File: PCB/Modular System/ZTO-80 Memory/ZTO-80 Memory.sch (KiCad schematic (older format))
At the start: 10 parts, among them J1 ZTO-80 Bus, J2 Conn_01x02, U1 28C256, U2 AS6C62256, U3 74HC139

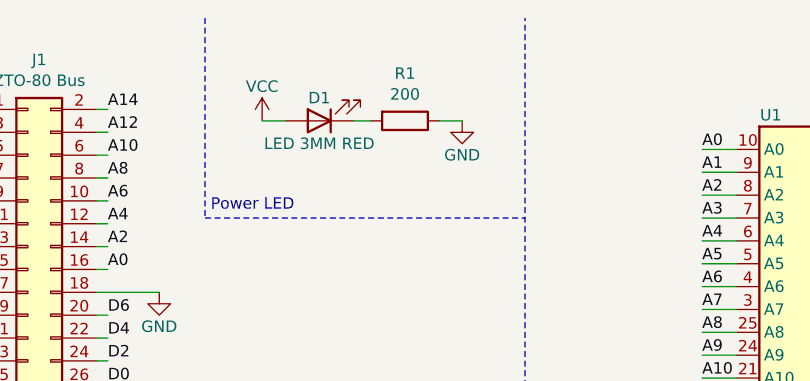
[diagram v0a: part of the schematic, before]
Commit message: Edited power LED resistor value
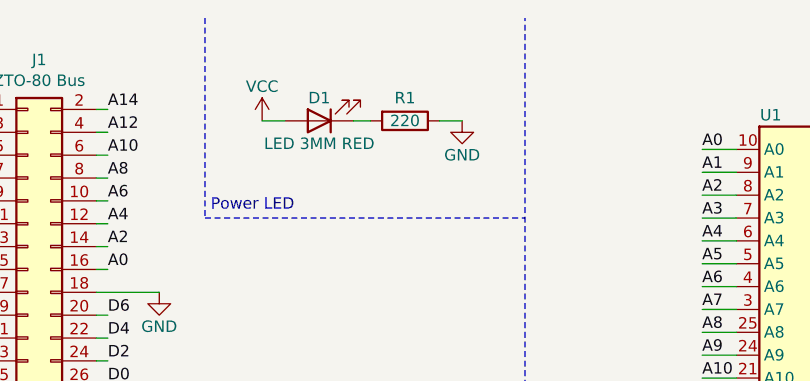
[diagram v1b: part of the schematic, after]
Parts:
- R1: value 200 -> 220
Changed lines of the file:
@@
 U 1 1 5E2B6523
 P 2825 925
-F 0 "R1" V 2618 925 50  0000 C CNN
-F 1 "200" V 2709 925 50  0000 C CNN
+F 0 "R1" V 2725 925 50  0000 C CNN
+F 1 "220" V 2825 925 50  0000 C CNN
 F 2 "Resistor_SMD:R_0805_2012Metric_Pad1.15x1.40mm_HandSolder" V 2755 925 50  0001 C CNN
 F 3 "~" H 2825 925 50  0001 C CNN

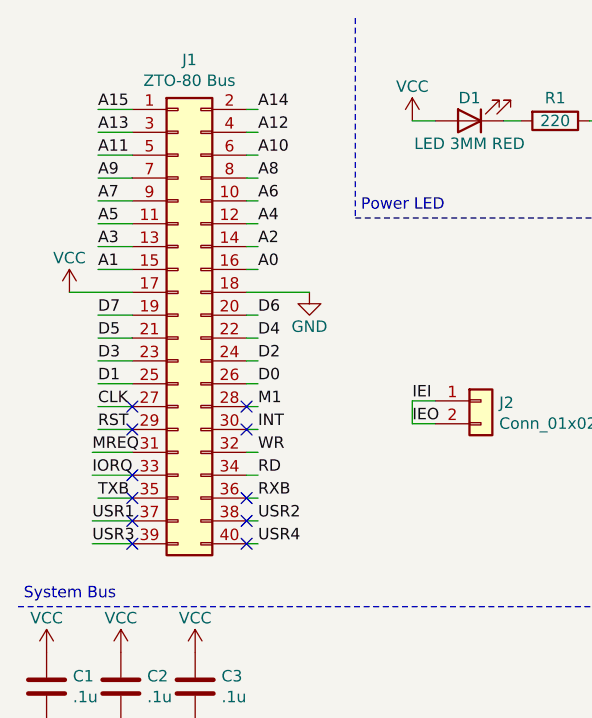
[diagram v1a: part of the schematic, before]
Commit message: Changed bus orientation
This change is backwards-compatible with all previous ZTO-80 modules
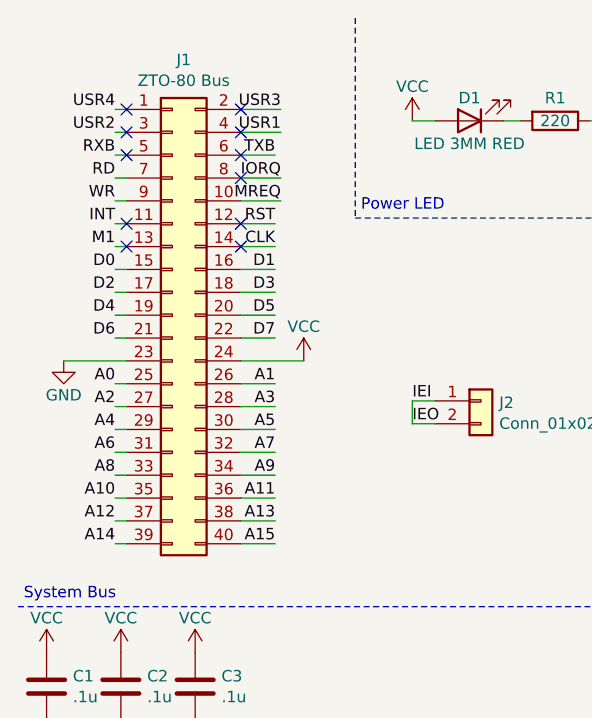
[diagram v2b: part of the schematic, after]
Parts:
- J1: footprint ZTO-80_Header:PinHeader_2x20_P2.54mm_Horizontal -> Connector_PinHeader_2.54mm:PinHeader_2x20_P2.54mm_Horizontal
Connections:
- net A0: now also J1.25 (Pin_25); no longer J1.16 (Pin_16)
- net A1: now also J1.26 (Pin_26); no longer J1.15 (Pin_15)
- net A10: now also J1.35 (Pin_35); no longer J1.6 (Pin_6)
- net A11: now also J1.36 (Pin_36); no longer J1.5 (Pin_5)
- net A12: now also J1.37 (Pin_37); no longer J1.4 (Pin_4)
- net A13: now also J1.38 (Pin_38); no longer J1.3 (Pin_3)
- net A14: now also J1.39 (Pin_39); no longer J1.2 (Pin_2)
- net A15: now also J1.40 (Pin_40); no longer J1.1 (Pin_1)
- net A2: now also J1.27 (Pin_27); no longer J1.14 (Pin_14)
- net A3: now also J1.28 (Pin_28); no longer J1.13 (Pin_13)
- net A4: now also J1.29 (Pin_29); no longer J1.12 (Pin_12)
- net A5: now also J1.30 (Pin_30); no longer J1.11 (Pin_11)
- net A6: now also J1.31 (Pin_31); no longer J1.10 (Pin_10)
- net A7: now also J1.32 (Pin_32); no longer J1.9 (Pin_9)
- net A8: now also J1.33 (Pin_33); no longer J1.8 (Pin_8)
- net A9: now also J1.34 (Pin_34); no longer J1.7 (Pin_7)
- net CLK: now also J1.14 (Pin_14); no longer J1.27 (Pin_27)
- net D0: now also J1.15 (Pin_15); no longer J1.26 (Pin_26)
- net D1: now also J1.16 (Pin_16); no longer J1.25 (Pin_25)
- net D2: now also J1.17 (Pin_17); no longer J1.24 (Pin_24)
- net D3: now also J1.18 (Pin_18); no longer J1.23 (Pin_23)
- net D4: now also J1.19 (Pin_19); no longer J1.22 (Pin_22)
- net D5: now also J1.20 (Pin_20); no longer J1.21 (Pin_21)
- net D6: now also J1.21 (Pin_21); no longer J1.20 (Pin_20)
- net D7: now also J1.22 (Pin_22); no longer J1.19 (Pin_19)
- net GND: now also J1.23 (Pin_23); no longer J1.18 (Pin_18)
- net INT: now also J1.11 (Pin_11); no longer J1.30 (Pin_30)
- net IORQ: now also J1.8 (Pin_8); no longer J1.33 (Pin_33)
- net M1: now also J1.13 (Pin_13); no longer J1.28 (Pin_28)
- net MREQ: now also J1.10 (Pin_10); no longer J1.31 (Pin_31)
- net RD: now also J1.7 (Pin_7); no longer J1.34 (Pin_34)
- net RST: now also J1.12 (Pin_12); no longer J1.29 (Pin_29)
- net RXB: now also J1.5 (Pin_5); no longer J1.36 (Pin_36)
- net TXB: now also J1.6 (Pin_6); no longer J1.35 (Pin_35)
- net USR1: now also J1.4 (Pin_4); no longer J1.37 (Pin_37)
- net USR2: now also J1.3 (Pin_3); no longer J1.38 (Pin_38)
- net USR3: now also J1.2 (Pin_2); no longer J1.39 (Pin_39)
- net USR4: now also J1.1 (Pin_1); no longer J1.40 (Pin_40)
- net VCC: now also J1.24 (Pin_24); no longer J1.17 (Pin_17)
- net WR: now also J1.9 (Pin_9); no longer J1.32 (Pin_32)
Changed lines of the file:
@@
 Comment4 ""
 $EndDescr
-Wire Wire Line
-	825  2575 975  2575
-Wire Wire Line
-	800  2675 975  2675
-Wire Wire Line
-	800  2775 975  2775
-$Comp
-L Connector_Generic:Conn_02x20_Odd_Even J1
-U 1 1 5E25F961
-P 1175 1775
-F 0 "J1" H 1225 2892 50  0000 C CNN
-F 1 "ZTO-80 Bus" H 1225 2801 50  0000 C CNN
-F 2 "ZTO-80_Header:PinHeader_2x20_P2.54mm_Horizontal" H 1175 1775 50  0001 C CNN
-F 3 "~" H 1175 1775 50  0001 C CNN
-	1    1175 1775
-	1    0    0    -1
-$EndComp
-Wire Wire Line
-	975  875  825  875
-Wire Wire Line
-	975  975  825  975
-Wire Wire Line
-	975  1075 825  1075
-Wire Wire Line
-	975  1175 825  1175
-Wire Wire Line
-	975  1275 825  1275
-Wire Wire Line
-	975  1375 825  1375
-Wire Wire Line
-	975  1475 825  1475
-Wire Wire Line
-	975  1575 825  1575
-Wire Wire Line
-	975  1775 825  1775
-Wire Wire Line
-	975  1875 825  1875
-Wire Wire Line
-	975  1975 825  1975
-Wire Wire Line
-	975  2075 825  2075
-Wire Wire Line
-	975  2175 825  2175
-Wire Wire Line
-	975  2275 825  2275
-Text Label 1525 1575 0    50   ~ 0
-A0
-Text Label 825  1575 0    50   ~ 0
-A1
-Text Label 1525 1475 0    50   ~ 0
-A2
-Text Label 825  1475 0    50   ~ 0
-A3
-Text Label 1525 1375 0    50   ~ 0
-A4
-Text Label 825  1375 0    50   ~ 0
-A5
-Text Label 1525 1275 0    50   ~ 0
-A6
-Text Label 825  1275 0    50   ~ 0
-A7
-Text Label 1525 1175 0    50   ~ 0
-A8
-Text Label 825  1175 0    50   ~ 0
-A9
-Text Label 1525 1075 0    50   ~ 0
-A10
-Text Label 825  1075 0    50   ~ 0
-A11
-Text Label 1525 975  0    50   ~ 0
-A12
-Text Label 825  975  0    50   ~ 0
-A13
-Text Label 1525 875  0    50   ~ 0
-A14
-Text Label 825  875  0    50   ~ 0
-A15
-$Comp
-L power:VCC #PWR01
-U 1 1 5E287266
-P 700 1675
-F 0 "#PWR01" H 700 1525 50  0001 C CNN
-F 1 "VCC" H 700 1825 50  0000 C CNN
-F 2 "" H 700 1675 50  0001 C CNN
-F 3 "" H 700 1675 50  0001 C CNN
-	1    700  1675
-	1    0    0    -1
-$EndComp
-Wire Wire Line
-	700  1675 975  1675
-$Comp
-L power:GND #PWR02
-U 1 1 5E288EF4
-P 1750 1675
-F 0 "#PWR02" H 1750 1425 50  0001 C CNN
-F 1 "GND" H 1750 1525 50  0000 C CNN
-F 2 "" H 1750 1675 50  0001 C CNN
-F 3 "" H 1750 1675 50  0001 C CNN
-	1    1750 1675
-	1    0    0    -1
-$EndComp
-Wire Wire Line
-	1475 875  1525 875
-Wire Wire Line
-	1475 975  1525 975
-Wire Wire Line
-	1475 1075 1525 1075
-Wire Wire Line
-	1475 1175 1525 1175
-Wire Wire Line
-	1475 1275 1525 1275
-Wire Wire Line
-	1475 1375 1525 1375
-Wire Wire Line
-	1475 1475 1525 1475
-Wire Wire Line
-	1475 1575 1525 1575
-Wire Wire Line
-	1475 1775 1525 1775
-Wire Wire Line
-	1475 1875 1525 1875
-Wire Wire Line
-	1475 1975 1525 1975
-Wire Wire Line
-	1475 2075 1525 2075
-Wire Wire Line
-	1475 2175 1525 2175
-Wire Wire Line
-	1475 2275 1525 2275
-Wire Wire Line
-	1475 2375 1525 2375
-Wire Wire Line
-	1475 2475 1525 2475
-Wire Wire Line
-	1475 2575 1525 2575
-Wire Wire Line
-	1475 2675 1525 2675
-Wire Wire Line
-	1475 2775 1525 2775
-Wire Wire Line
-	1475 1675 1750 1675
-Text Label 825  2075 0    50   ~ 0
-D1
-Text Label 1525 1975 0    50   ~ 0
-D2
-Text Label 825  1975 0    50   ~ 0
-D3
-Text Label 1525 1875 0    50   ~ 0
-D4
-Text Label 1525 1775 0    50   ~ 0
-D6
-Text Label 825  1775 0    50   ~ 0
-D7
-Text Label 1525 2075 0    50   ~ 0
-D0
-Text Label 825  1875 0    50   ~ 0
-D5
-Text Label 825  2175 0    50   ~ 0
-CLK
-Text Label 1525 2175 0    50   ~ 0
-M1
-Text Label 825  2275 0    50   ~ 0
-RST
-Text Label 1525 2275 0    50   ~ 0
-INT
-Text Label 800  2375 0    50   ~ 0
-MREQ
-Wire Wire Line
-	800  2375 975  2375
-Text Label 1525 2375 0    50   ~ 0
-WR
-Text Label 800  2475 0    50   ~ 0
-IORQ
-Wire Wire Line
-	800  2475 975  2475
-Text Label 1525 2475 0    50   ~ 0
-RD
-Text Label 825  2575 0    50   ~ 0
-TXB
-Text Label 1525 2575 0    50   ~ 0
-RXB
-Text Label 1525 2675 0    50   ~ 0
-USR2
-Text Label 800  2775 0    50   ~ 0
-USR3
-Text Label 1525 2775 0    50   ~ 0
-USR4
-Text Label 800  2675 0    50   ~ 0
-USR1
 $Comp
 L power:PWR_FLAG #FLG01
@@
 	1    0    0    -1
 $EndComp
-NoConn ~ 1475 2775
-NoConn ~ 1475 2675
-NoConn ~ 1475 2575
-NoConn ~ 1475 2275
-NoConn ~ 1475 2175
-NoConn ~ 975  2175
-NoConn ~ 975  2275
-NoConn ~ 975  2475
-NoConn ~ 975  2575
-NoConn ~ 975  2675
-NoConn ~ 975  2775
 Wire Wire Line
 	2200 2250 2200 2150
+Wire Wire Line
+	1600 1075 1450 1075
+Wire Wire Line
+	1625 975  1450 975
+Wire Wire Line
+	1625 875  1450 875
+Wire Wire Line
+	1450 2775 1600 2775
+Wire Wire Line
+	1450 2675 1600 2675
+Wire Wire Line
+	1450 2575 1600 2575
+Wire Wire Line
+	1450 2475 1600 2475
+Wire Wire Line
+	1450 2375 1600 2375
+Wire Wire Line
+	1450 2275 1600 2275
+Wire Wire Line
+	1450 2175 1600 2175
+Wire Wire Line
+	1450 2075 1600 2075
+Wire Wire Line
+	1450 1875 1600 1875
+Wire Wire Line
+	1450 1775 1600 1775
+Wire Wire Line
+	1450 1675 1600 1675
+Wire Wire Line
+	1450 1575 1600 1575
+Wire Wire Line
+	1450 1475 1600 1475
+Wire Wire Line
+	1450 1375 1600 1375
+Text Label 900  2075 2    50   ~ 0
+A0
+Text Label 1600 2075 2    50   ~ 0
+A1
+Text Label 900  2175 2    50   ~ 0
+A2
+Text Label 1600 2175 2    50   ~ 0
+A3
+Text Label 900  2275 2    50   ~ 0
+A4
+Text Label 1600 2275 2    50   ~ 0
+A5
+Text Label 900  2375 2    50   ~ 0
+A6
+Text Label 1600 2375 2    50   ~ 0
+A7
+Text Label 900  2475 2    50   ~ 0
+A8
+Text Label 1600 2475 2    50   ~ 0
+A9
+Text Label 900  2575 2    50   ~ 0
+A10
+Text Label 1600 2575 2    50   ~ 0
+A11
+Text Label 900  2675 2    50   ~ 0
+A12
+Text Label 1600 2675 2    50   ~ 0
+A13
+Text Label 900  2775 2    50   ~ 0
+A14
+Text Label 1600 2775 2    50   ~ 0
+A15
+$Comp
+L power:VCC #PWR02
+U 1 1 5F424DFE
+P 1725 1975
+F 0 "#PWR02" H 1725 1825 50  0001 C CNN
+F 1 "VCC" H 1725 2125 50  0000 C CNN
+F 2 "" H 1725 1975 50  0001 C CNN
+F 3 "" H 1725 1975 50  0001 C CNN
+	1    1725 1975
+	1    0    0    -1
+$EndComp
+Wire Wire Line
+	1725 1975 1450 1975
+$Comp
+L power:GND #PWR01
+U 1 1 5F424E05
+P 675 1975
+F 0 "#PWR01" H 675 1725 50  0001 C CNN
+F 1 "GND" H 675 1825 50  0000 C CNN
+F 2 "" H 675 1975 50  0001 C CNN
+F 3 "" H 675 1975 50  0001 C CNN
+	1    675  1975
+	1    0    0    -1
+$EndComp
+Wire Wire Line
+	950  2775 900  2775
+Wire Wire Line
+	950  2675 900  2675
+Wire Wire Line
+	950  2575 900  2575
+Wire Wire Line
+	950  2475 900  2475
+Wire Wire Line
+	950  2375 900  2375
+Wire Wire Line
+	950  2275 900  2275
+Wire Wire Line
+	950  2175 900  2175
+Wire Wire Line
+	950  2075 900  2075
+Wire Wire Line
+	950  1875 900  1875
+Wire Wire Line
+	950  1775 900  1775
+Wire Wire Line
+	950  1675 900  1675
+Wire Wire Line
+	950  1575 900  1575
+Wire Wire Line
+	950  1475 900  1475
+Wire Wire Line
+	950  1375 900  1375
+Wire Wire Line
+	950  1275 900  1275
+Wire Wire Line
+	950  1175 900  1175
+Wire Wire Line
+	950  1075 900  1075
+Wire Wire Line
+	950  975  900  975
+Wire Wire Line
+	950  875  900  875
+Wire Wire Line
+	950  1975 675  1975
+Text Label 1600 1575 2    50   ~ 0
+D1
+Text Label 900  1675 2    50   ~ 0
+D2
+Text Label 1600 1675 2    50   ~ 0
+D3
+Text Label 900  1775 2    50   ~ 0
+D4
+Text Label 900  1875 2    50   ~ 0
+D6
+Text Label 1600 1875 2    50   ~ 0
+D7
+Text Label 900  1575 2    50   ~ 0
+D0
+Text Label 1600 1775 2    50   ~ 0
+D5
+Text Label 1600 1475 2    50   ~ 0
+CLK
+Text Label 900  1475 2    50   ~ 0
+M1
+Text Label 1600 1375 2    50   ~ 0
+RST
+Text Label 900  1375 2    50   ~ 0
+INT
+Text Label 1625 1275 2    50   ~ 0
+MREQ
+Wire Wire Line
+	1625 1275 1450 1275
+Text Label 900  1275 2    50   ~ 0
+WR
+Text Label 1625 1175 2    50   ~ 0
+IORQ
+Wire Wire Line
+	1625 1175 1450 1175
+Text Label 900  1175 2    50   ~ 0
+RD
+Text Label 1600 1075 2    50   ~ 0
+TXB
+Text Label 900  1075 2    50   ~ 0
+RXB
+Text Label 900  975  2    50   ~ 0
+USR2
+Text Label 1625 875  2    50   ~ 0
+USR3
+Text Label 900  875  2    50   ~ 0
+USR4
+Text Label 1625 975  2    50   ~ 0
+USR1
+$Comp
+L Connector_Generic:Conn_02x20_Odd_Even J1
+U 1 1 5F424E37
+P 1150 1775
+F 0 "J1" H 1200 2892 50  0000 C CNN
+F 1 "ZTO-80 Bus" H 1200 2801 50  0000 C CNN
+F 2 "Connector_PinHeader_2.54mm:PinHeader_2x20_P2.54mm_Horizontal" H 1150 1775 50  0001 C CNN
+F 3 "~" H 1150 1775 50  0001 C CNN
+	1    1150 1775
+	1    0    0    -1
+$EndComp
+NoConn ~ 1450 875
+NoConn ~ 1450 975
+NoConn ~ 1450 1075
+NoConn ~ 1450 1175
+NoConn ~ 950  1075
+NoConn ~ 950  975
+NoConn ~ 950  875
+NoConn ~ 1450 1375
+NoConn ~ 1450 1475
+NoConn ~ 950  1375
+NoConn ~ 950  1475
 $EndSCHEMATC
